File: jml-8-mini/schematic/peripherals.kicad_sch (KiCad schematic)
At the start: 9 parts, among them J2 SIO CHB, J3 UART, J4 CTC Extra Lines, U4 Z80CTC, U5 Z80SIO

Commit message: change "JML-8 Mini" to "JML-8-Mini" in schematic description
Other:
- title: JML-8 Mini Schematic -> JML-8-Mini Schematic
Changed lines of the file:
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@@
   (paper "A4")
   (title_block
-    (title "JML-8 Mini Schematic")
+    (title "JML-8-Mini Schematic")
     (date "2023-10-02")
     (rev "A")

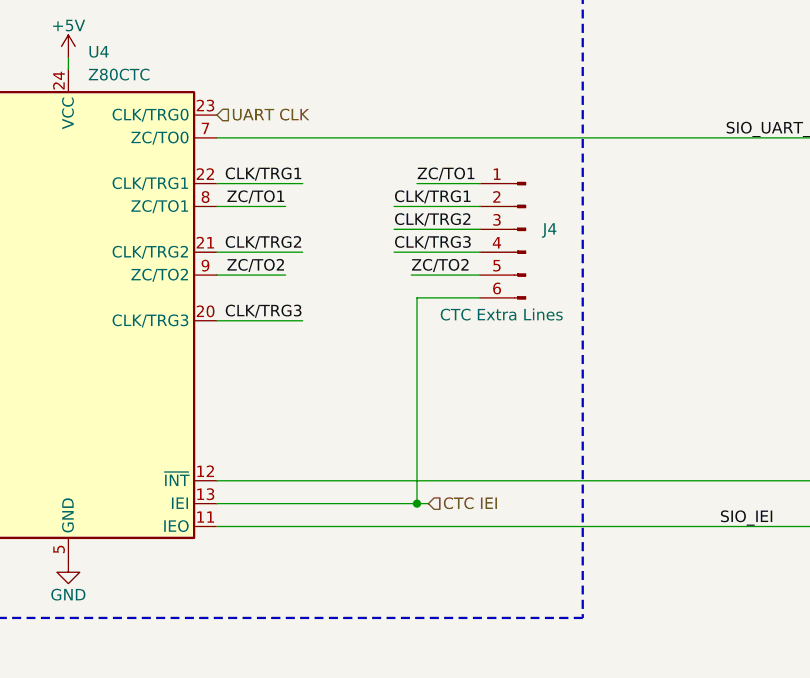
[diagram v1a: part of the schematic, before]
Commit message: remove CTC header pins, start Rev B
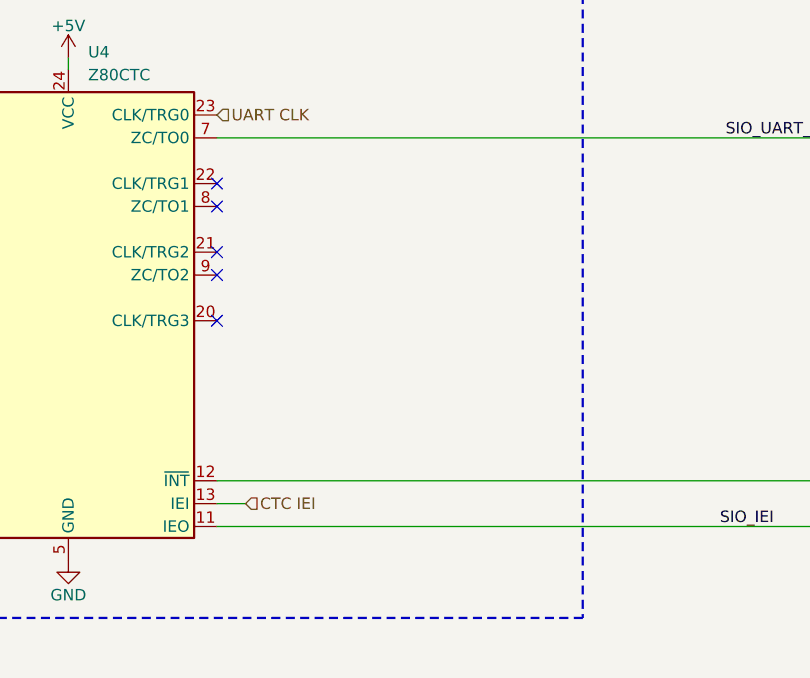
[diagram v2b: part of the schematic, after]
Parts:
- removed J4: CTC Extra Lines, Connector_PinHeader_2.54mm:PinHeader_1x06_P2.54mm_Vertical, symbol Connector:Conn_01x06_Pin
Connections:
- net CLK/TRG1: no longer names the net of U4.22 (CLK/TRG1)
- net CLK/TRG2: no longer names the net of U4.21 (CLK/TRG2)
- net CLK/TRG3: no longer names the net of U4.20 (CLK/TRG3)
- net ZC/TO1: no longer names the net of U4.8 (ZC/TO1)
- net ZC/TO2: no longer names the net of U4.9 (ZC/TO2)
- no-connect marks 2 -> 7
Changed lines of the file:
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@@
   (title_block
     (title "JML-8-Mini Schematic")
-    (date "2023-10-02")
-    (rev "A")
+    (date "2023-10-20")
+    (rev "B")
     (company "https://github.com/jac-oblong/JML")
     (comment 1 "Design of Z80 based microcomputer")
@@
   (junction (at 48.895 107.315) (diameter 0) (color 0 0 0 0)
   )
-  (junction (at 118.11 81.915) (diameter 0) (color 0 0 0 0)
-  )
   (junction (at 235.585 64.135) (diameter 0) (color 0 0 0 0)
   )
+  (no_connect (at 95.885 46.355))
+  (no_connect (at 95.885 48.895))
+  (no_connect (at 95.885 53.975))
   (no_connect (at 234.95 56.515))
+  (no_connect (at 95.885 61.595))
   (no_connect (at 234.95 51.435))
+  (no_connect (at 95.885 56.515))
   (bus_entry (at 186.69 56.515) (size -2.54 2.54)
     (stroke (width 0) (type default))
@@
     (stroke (width 0) (type default))
   )
-  (wire (pts (xy 118.11 59.055) (xy 118.11 81.915))
-    (stroke (width 0) (type default))
-  )
   (wire (pts (xy 235.585 59.055) (xy 235.585 64.135))
     (stroke (width 0) (type default))
@@
     (stroke (width 0) (type default))
   )
-  (wire (pts (xy 115.57 51.435) (xy 125.095 51.435))
-    (stroke (width 0) (type default))
-  )
   (wire (pts (xy 218.44 107.315) (xy 218.44 108.585))
     (stroke (width 0) (type default))
@@
     (stroke (width 0) (type default))
   )
-  (wire (pts (xy 119.38 81.915) (xy 118.11 81.915))
-    (stroke (width 0) (type default))
-  )
-  (wire (pts (xy 115.57 48.895) (xy 125.095 48.895))
+  (wire (pts (xy 95.885 81.915) (xy 99.06 81.915))
     (stroke (width 0) (type default))
   )
@@
     (stroke (width 0) (type default))
   )
-  (wire (pts (xy 95.885 48.895) (xy 103.505 48.895))
-    (stroke (width 0) (type default))
-  )
   (wire (pts (xy 234.95 92.075) (xy 240.03 92.075))
     (stroke (width 0) (type default))
@@
     (stroke (width 0) (type default))
   )
-  (wire (pts (xy 117.475 56.515) (xy 125.095 56.515))
-    (stroke (width 0) (type default))
-  )
   (bus (pts (xy 48.895 46.355) (xy 48.895 48.895))
     (stroke (width 0) (type default))
@@
     (stroke (width 0) (type default))
   )
-  (wire (pts (xy 95.885 53.975) (xy 105.41 53.975))
-    (stroke (width 0) (type default))
-  )
   (wire (pts (xy 234.95 61.595) (xy 243.84 61.595))
     (stroke (width 0) (type default))
@@
     (stroke (width 0) (type default))
   )
-  (wire (pts (xy 115.57 53.975) (xy 125.095 53.975))
-    (stroke (width 0) (type default))
-  )
   (wire (pts (xy 248.285 43.815) (xy 234.95 43.815))
     (stroke (width 0) (type default))
@@
     (stroke (width 0) (type default))
   )
-  (wire (pts (xy 95.885 46.355) (xy 105.41 46.355))
-    (stroke (width 0) (type default))
-  )
   (wire (pts (xy 194.31 69.215) (xy 201.93 69.215))
     (stroke (width 0) (type default))
@@
     (stroke (width 0) (type default))
   )
-  (wire (pts (xy 95.885 81.915) (xy 118.11 81.915))
-    (stroke (width 0) (type default))
-  )
   (bus (pts (xy 184.15 59.055) (xy 184.15 107.315))
     (stroke (width 0) (type default))
@@
     (stroke (width 0) (type default))
   )
-  (wire (pts (xy 95.885 61.595) (xy 105.41 61.595))
-    (stroke (width 0) (type default))
-  )
   (wire (pts (xy 201.93 46.355) (xy 186.69 46.355))
     (stroke (width 0) (type default))
@@
     (stroke (width 0) (type default))
   )
-  (wire (pts (xy 125.095 59.055) (xy 118.11 59.055))
-    (stroke (width 0) (type default))
-  )
   (wire (pts (xy 194.31 79.375) (xy 201.93 79.375))
     (stroke (width 0) (type default))
@@
     (stroke (width 0) (type default))
   )
-  (wire (pts (xy 118.11 46.355) (xy 125.095 46.355))
-    (stroke (width 0) (type default))
-  )
   (wire (pts (xy 254.635 76.835) (xy 260.985 76.835))
-    (stroke (width 0) (type default))
-  )
-  (wire (pts (xy 95.885 56.515) (xy 103.505 56.515))
     (stroke (width 0) (type default))
   )
@@
     (effects (font (size 1.27 1.27)) (justify left bottom))
   )
-  (label "CLK{slash}TRG3" (at 105.41 61.595 180) (fields_autoplaced)
-    (effects (font (size 1.27 1.27)) (justify right bottom))
-  )
   (label "D6" (at 189.23 53.975 180) (fields_autoplaced)
     (effects (font (size 1.27 1.27)) (justify right bottom))
   )
-  (label "CLK{slash}TRG2" (at 105.41 53.975 180) (fields_autoplaced)
-    (effects (font (size 1.27 1.27)) (justify right bottom))
-  )
   (label "TxDA" (at 236.855 43.815 0) (fields_autoplaced)
     (effects (font (size 1.27 1.27)) (justify left bottom))
@@
     (effects (font (size 1.27 1.27)) (justify left bottom))
   )
-  (label "ZC{slash}TO1" (at 118.11 46.355 0) (fields_autoplaced)
-    (effects (font (size 1.27 1.27)) (justify left bottom))
-  )
   (label "D3" (at 189.23 46.355 180) (fields_autoplaced)
     (effects (font (size 1.27 1.27)) (justify right bottom))
@@
     (effects (font (size 1.27 1.27)) (justify right bottom))
   )
-  (label "ZC{slash}TO2" (at 103.505 56.515 180) (fields_autoplaced)
-    (effects (font (size 1.27 1.27)) (justify right bottom))
-  )
-  (label "CLK{slash}TRG1" (at 105.41 46.355 180) (fields_autoplaced)
-    (effects (font (size 1.27 1.27)) (justify right bottom))
-  )
   (label "~{IORQ}" (at 56.515 69.215 0) (fields_autoplaced)
     (effects (font (size 1.27 1.27)) (justify left bottom))
@@
     (effects (font (size 1.27 1.27)) (justify left bottom))
   )
-  (label "CLK{slash}TRG3" (at 115.57 53.975 0) (fields_autoplaced)
-    (effects (font (size 1.27 1.27)) (justify left bottom))
-  )
   (label "D2" (at 189.23 43.815 180) (fields_autoplaced)
     (effects (font (size 1.27 1.27)) (justify right bottom))
@@
     (effects (font (size 1.27 1.27)) (justify right bottom))
   )
-  (label "ZC{slash}TO2" (at 117.475 56.515 0) (fields_autoplaced)
-    (effects (font (size 1.27 1.27)) (justify left bottom))
-  )
   (label "SIO_IEO" (at 194.31 84.455 0) (fields_autoplaced)
     (effects (font (size 1.27 1.27)) (justify left bottom))
@@
     (effects (font (size 1.27 1.27)) (justify right bottom))
   )
-  (label "CLK{slash}TRG1" (at 115.57 48.895 0) (fields_autoplaced)
-    (effects (font (size 1.27 1.27)) (justify left bottom))
-  )
   (label "SIO_UART_CLK" (at 152.4 41.275 0) (fields_autoplaced)
     (effects (font (size 1.27 1.27)) (justify left bottom))
@@
   )
   (label "TxDB" (at 256.54 84.455 0) (fields_autoplaced)
-    (effects (font (size 1.27 1.27)) (justify left bottom))
-  )
-  (label "ZC{slash}TO1" (at 103.505 48.895 180) (fields_autoplaced)
-    (effects (font (size 1.27 1.27)) (justify right bottom))
-  )
-  (label "CLK{slash}TRG2" (at 115.57 51.435 0) (fields_autoplaced)
     (effects (font (size 1.27 1.27)) (justify left bottom))
   )
@@
     (effects (font (size 1.27 1.27)) (justify right))
   )
-  (hierarchical_label "CTC IEI" (shape input) (at 119.38 81.915 0) (fields_autoplaced)
+  (hierarchical_label "CTC IEI" (shape input) (at 99.06 81.915 0) (fields_autoplaced)
     (effects (font (size 1.27 1.27)) (justify left))
   )
@@
         )
       )
-    )
-  )
-  (symbol (lib_id "Connector:Conn_01x06_Pin") (at 130.175 51.435 0) (mirror y) (unit 1)
-    (in_bom yes) (on_board yes) (dnp no)
-    (property "Reference" "J4" (at 132.08 51.435 0)
-      (effects (font (size 1.27 1.27)) (justify right))
-    )
-    (property "Value" "CTC Extra Lines" (at 120.65 60.96 0)
-      (effects (font (size 1.27 1.27)) (justify right))
-    )
-    (property "Footprint" "Connector_PinHeader_2.54mm:PinHeader_1x06_P2.54mm_Vertical" (at 130.175 51.435 0)
-      (effects (font (size 1.27 1.27)) hide)
-    )
-    (property "Datasheet" "~" (at 130.175 51.435 0)
-      (effects (font (size 1.27 1.27)) hide)
-    )
-    (pin "1")
-    (pin "2")
-    (pin "3")
-    (pin "4")
-    (pin "5")
-    (pin "6")
-    (instances
-      (project "jml-8-mini"
-        (path "/7f93abb4-2372-4a9e-a664-5edb67349db4/11c4238e-8051-4a00-8608-741a8b831ae1"
-          (reference "J4") (unit 1)
-        )
-      )

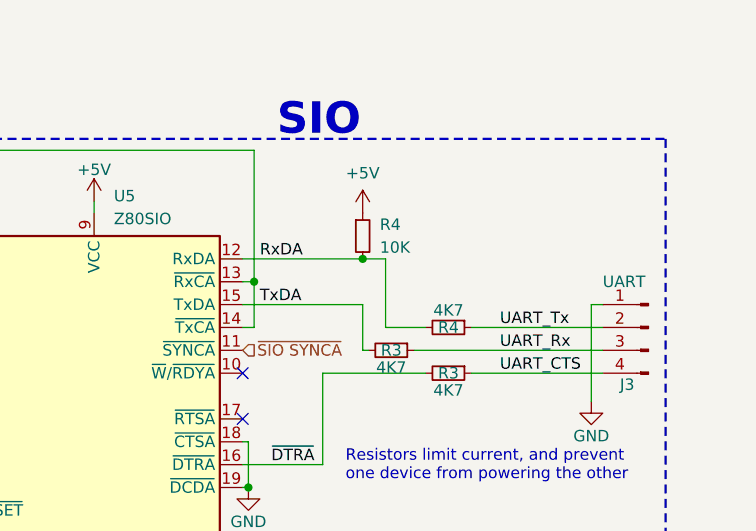
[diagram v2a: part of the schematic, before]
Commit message: fix incorrect value for resistor
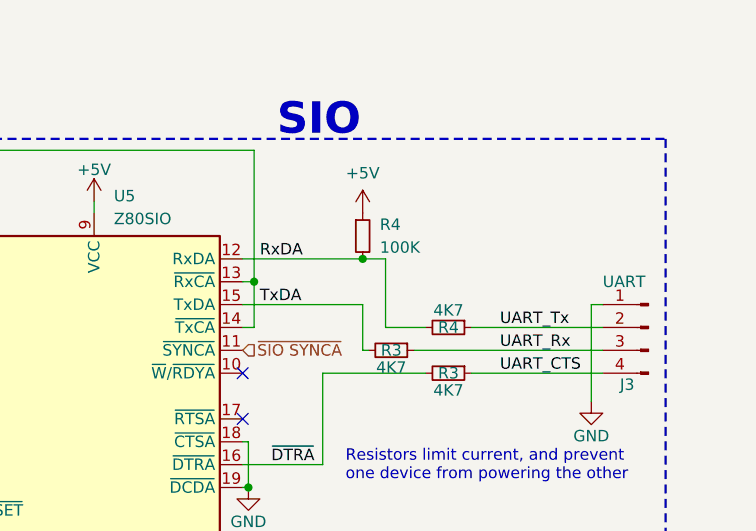
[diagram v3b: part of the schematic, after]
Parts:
- R4: value 10K -> 100K
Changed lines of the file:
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@@
       (effects (font (size 1.27 1.27)) (justify left))
     )
-    (property "Value" "10K" (at 250.19 37.465 0)
+    (property "Value" "100K" (at 250.19 37.465 0)
       (effects (font (size 1.27 1.27)) (justify left))
     )
